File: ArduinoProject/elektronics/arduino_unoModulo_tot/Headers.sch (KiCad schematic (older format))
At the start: 4 parts, among them P1 Power Header, P2 Analog Header, P3 Digital Header 02, P4 Digital Header 01

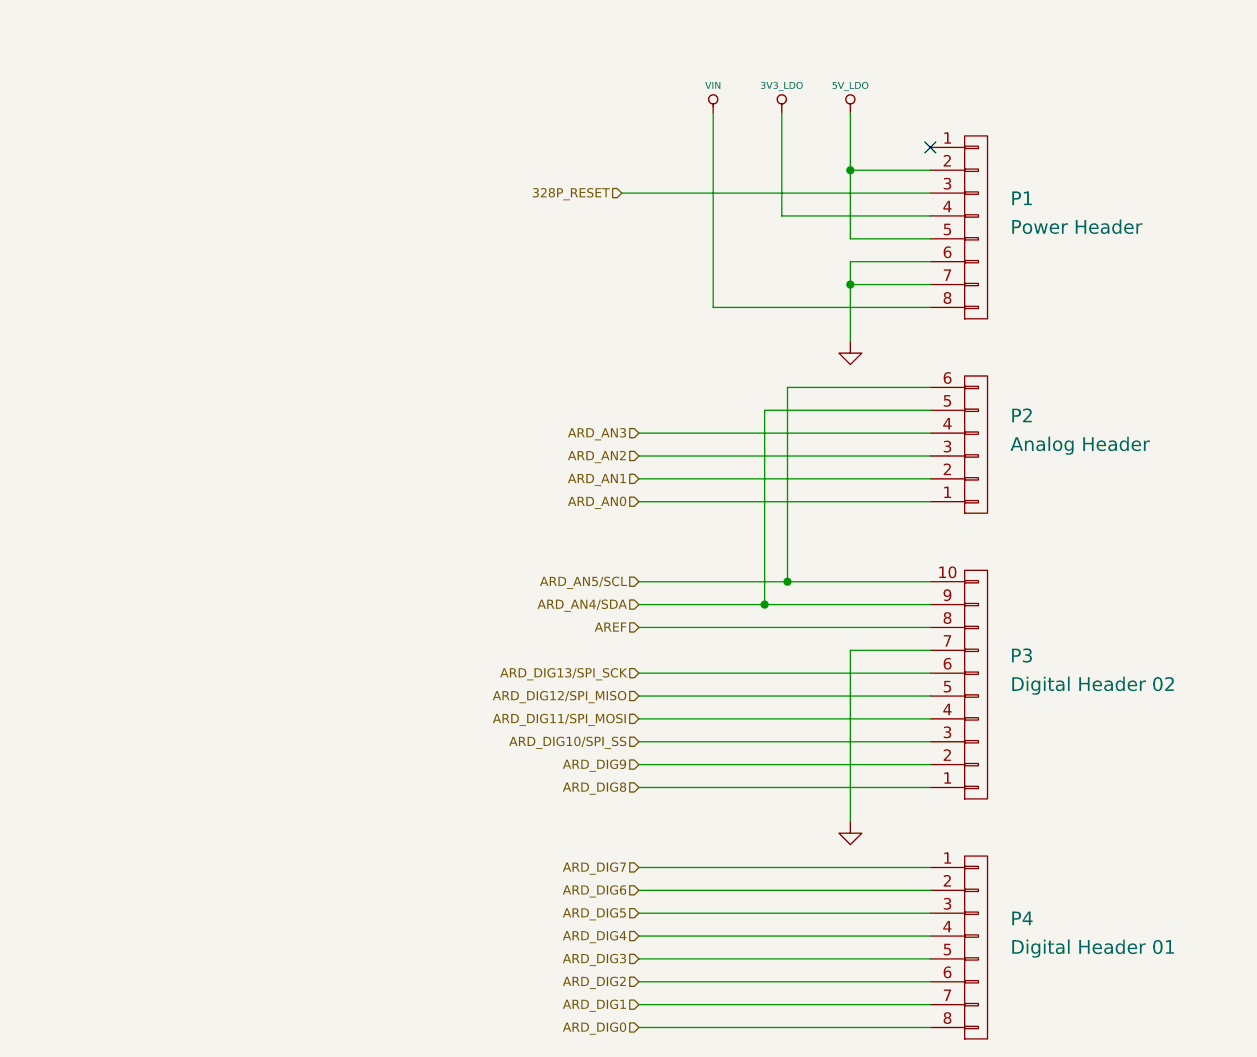
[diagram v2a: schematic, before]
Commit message: kicad schema altered: alles op 1 PCB2
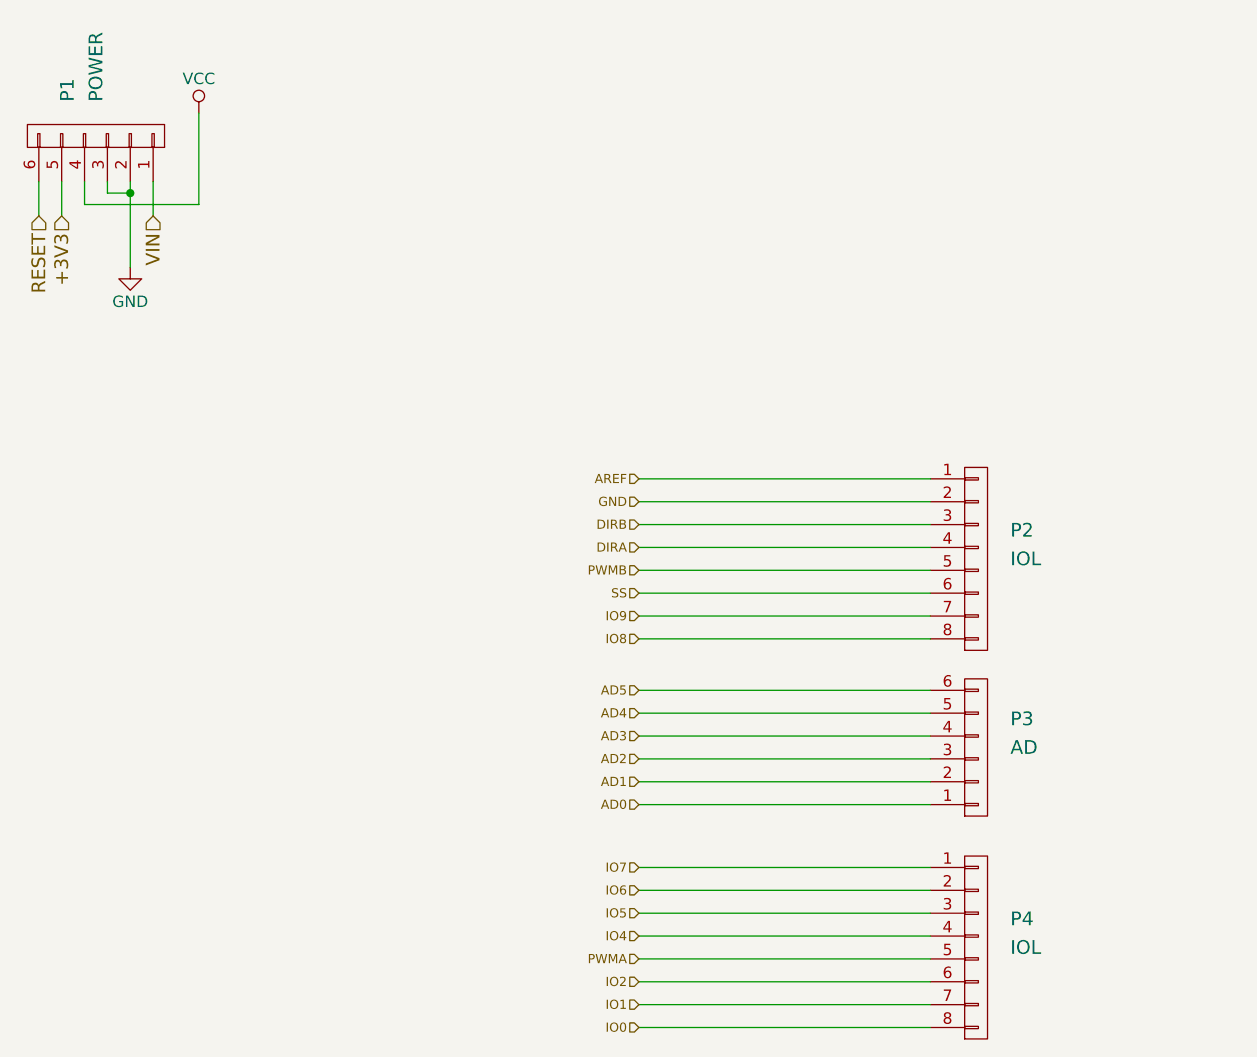
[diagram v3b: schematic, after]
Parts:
- removed P1: Power Header, Connectors_Phoenix:PhoenixContact_PTSM0,5_8-2,5-V_SMD, symbol CONN_01X08
- removed P3: Digital Header 02, Connectors_Phoenix:PhoenixContact_PTSM0,5_10-2,5-V_SMD, symbol CONN_01X10
- added P1: POWER, Connectors_Phoenix:PhoenixContact_PTSM0,5_6-2,5-V_SMD, symbol CONN_01X06
- added P2: IOL, Diodes_SMD:D_MELF-RM10_Universal_Handsoldering, symbol CONN_01X08
- P3: renamed from P2; value Analog Header -> AD
- P4: value Digital Header 01 -> IOL
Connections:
- net AREF: now also P2.1 (P1)
- net GND: now also P1.2 (P2), P1.3 (P3), P2.2 (P2)
- net ARD_AN0 renamed AD0
- net ARD_AN1 renamed AD1
- net ARD_AN2 renamed AD2
- net ARD_AN3 renamed AD3
- net ARD_AN4/SDA renamed AD4
- net ARD_AN5/SCL renamed AD5
- net ARD_DIG0 renamed IO0
- net ARD_DIG1 renamed IO1
- net ARD_DIG2 renamed IO2
- net ARD_DIG3 renamed PWMA
- net ARD_DIG4 renamed IO4
- net ARD_DIG5 renamed IO5
- net ARD_DIG6 renamed IO6
- net ARD_DIG7 renamed IO7
- new net +3V3: P1.5 (P5)
- new net DIRA: P2.4 (P4)
- new net DIRB: P2.3 (P3)
- new net IO8: P2.8 (P8)
- new net IO9: P2.7 (P7)
- new net PWMB: P2.5 (P5)
- new net RESET: P1.6 (P6)
- new net SS: P2.6 (P6)
- new net VCC: P1.4 (P4)
- new net VIN: P1.1 (P1)
- no-connect marks 1 -> 0
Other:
- moved on the sheet: P3

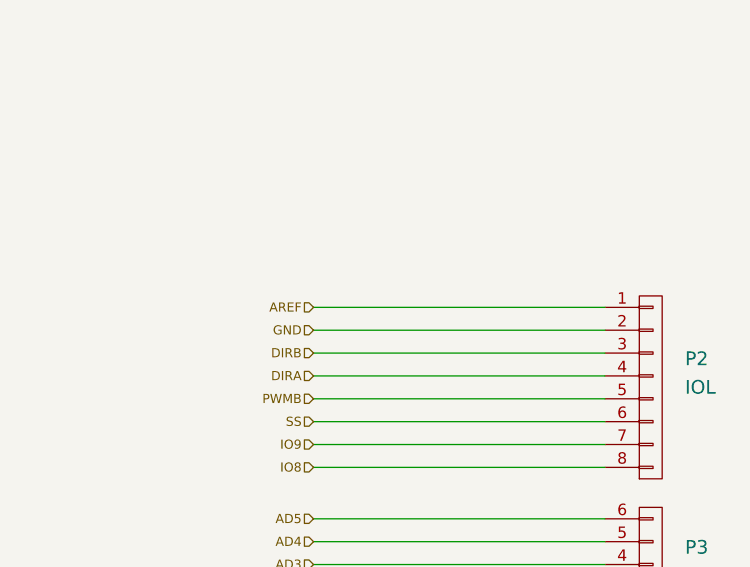
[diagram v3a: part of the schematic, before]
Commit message: kicad schema altered: alles op 1 PCB3
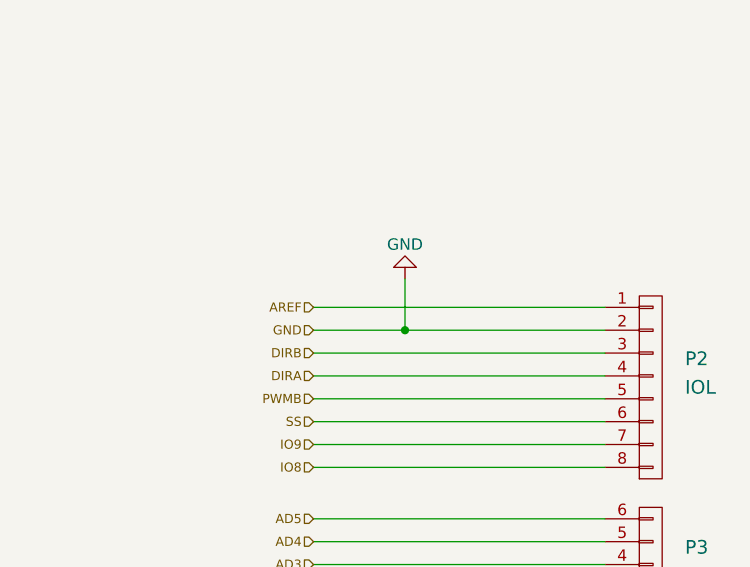
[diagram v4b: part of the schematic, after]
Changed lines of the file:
@@
 Text HLabel 2650 2325 3    60   Input ~ 0
 VIN
+Wire Wire Line
+	5175 3575 5175 3350
+Connection ~ 5175 3575
+$Comp
+L GND #PWR?
+U 1 1 5A9915EF
+P 5175 3350
+F 0 "#PWR?" H 5175 3100 50  0001 C CNN
+F 1 "GND" H 5175 3200 50  0000 C CNN
+F 2 "" H 5175 3350 50  0001 C CNN
+F 3 "" H 5175 3350 50  0001 C CNN
+	1    5175 3350
+	-1   0    0    1
+$EndComp
 $EndSCHEMATC
